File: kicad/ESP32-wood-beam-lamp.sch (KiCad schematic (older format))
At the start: 41 parts, among them J1 Screw_Terminal_01x05, J2 Screw_Terminal_01x05, J3 Conn_01x05_Male, J4 3.3 V, Q1 IRLZ44N, Q2 IRLZ44N, SW1 Flash, SW2 Reset, U1 TLV70233_SOT23-5, U2 ESP-WROOM-32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

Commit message: added BMP280
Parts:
- removed TP7: Test_Point, TestPoint:TestPoint_Pad_D1.0mm, symbol ESP32-wroom:Test_Point-Connector
- removed U4: Si7060-00, Package_TO_SOT_SMD:SOT-23-5, symbol ESP32-wroom:Si7060-module
- added U4: BMP280, symbol BMP280:BMP280
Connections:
- net labels removed: Alert2
- wire segments 146 -> 143
- no-connect marks 29 -> 30
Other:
- note removed: "Near Load Resistor\nAdress 00"
- moved on the sheet: C8
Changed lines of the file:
@@
-$EndComp
-$Comp
-L ESP32-wroom:Si7060-module U4
-U 1 1 5B338E05
-P 9150 4400
-F 0 "U4" H 9591 4471 50  0000 L CNN
-F 1 "Si7060-00" H 9591 4380 50  0000 L CNN
-F 2 "Package_TO_SOT_SMD:SOT-23-5" H 9150 4000 50  0001 C CNN
-F 3 "https://www.silabs.com/documents/public/data-sheets/Si7050-1-3-4-5-A20.pdf" H 8950 4700 50  0001 C CNN
-	1    9150 4400
-	1    0    0    -1
 $EndComp
 $Comp
@@
 L power:GND #PWR023
 U 1 1 5B340497
-P 9150 4800
-F 0 "#PWR023" H 9150 4550 50  0001 C CNN
-F 1 "GND" H 9155 4627 50  0000 C CNN
-F 2 "" H 9150 4800 50  0001 C CNN
-F 3 "" H 9150 4800 50  0001 C CNN
-	1    9150 4800
-	1    0    0    -1
-$EndComp
-Wire Wire Line
-	9150 4800 9150 4700
+P 9100 4800
+F 0 "#PWR023" H 9100 4550 50  0001 C CNN
+F 1 "GND" H 9105 4627 50  0000 C CNN
+F 2 "" H 9100 4800 50  0001 C CNN
+F 3 "" H 9100 4800 50  0001 C CNN
+	1    9100 4800
+	1    0    0    -1
+$EndComp
 $Comp
 L Device:R R12
@@
 $EndComp
 Wire Wire Line
-	8750 4300 8600 4300
+	8900 4300 8600 4300
 Wire Wire Line
 	8400 3800 8400 3900
 Wire Wire Line
 	8600 3800 8600 3900
-Wire Wire Line
-	9150 4050 9150 4000
-Wire Wire Line
-	9150 3800 8600 3800
 Connection ~ 8600 3800
 Wire Wire Line
@@
 Connection ~ 8400 4400
 Wire Wire Line
-	8400 4400 8750 4400
+	8400 4400 8900 4400
 Wire Wire Line
 	8600 4200 8600 4300
@@
 Wire Wire Line
 	8600 4300 8300 4300
-Text Label 9650 4550 0    50   ~ 0
-Alert2
-Text Label 3750 5200 0    50   ~ 0
-Alert2
-Wire Wire Line
-	3750 5200 3550 5200
 $Comp
 L power:GND #PWR010
@@
 L Device:C C8
 U 1 1 5B410ADA
-P 9600 4000
-F 0 "C8" H 9715 4046 50  0000 L CNN
-F 1 "100n" H 9715 3955 50  0000 L CNN
-F 2 "Capacitor_SMD:C_0603_1608Metric" H 9638 3850 50  0001 C CNN
-F 3 "~" H 9600 4000 50  0001 C CNN
-	1    9600 4000
+P 9650 3800
+F 0 "C8" H 9765 3846 50  0000 L CNN
+F 1 "100n" H 9765 3755 50  0000 L CNN
+F 2 "Capacitor_SMD:C_0603_1608Metric" H 9688 3650 50  0001 C CNN
+F 3 "~" H 9650 3800 50  0001 C CNN
+	1    9650 3800
 	0    1    1    0
 $EndComp
@@
 L power:GND #PWR025
 U 1 1 5B415F17
-P 9850 4000
-F 0 "#PWR025" H 9850 3750 50  0001 C CNN
-F 1 "GND" H 9855 3827 50  0000 C CNN
-F 2 "" H 9850 4000 50  0001 C CNN
-F 3 "" H 9850 4000 50  0001 C CNN
-	1    9850 4000
+P 9850 3800
+F 0 "#PWR025" H 9850 3550 50  0001 C CNN
+F 1 "GND" H 9855 3627 50  0000 C CNN
+F 2 "" H 9850 3800 50  0001 C CNN
+F 3 "" H 9850 3800 50  0001 C CNN
+	1    9850 3800
 	0    -1   -1   0
 $EndComp
 Wire Wire Line
-	9450 4000 9150 4000
-Connection ~ 9150 4000
-Wire Wire Line
-	9150 4000 9150 3800
-Wire Wire Line
-	9750 4000 9850 4000
-Text Notes 9450 3850 0    50   ~ 0
-Near Load Resistor\nAdress 00
+	9800 3800 9850 3800
 Text Notes 600  650  0    50   ~ 0
 Voltage Regulator
@@
 Wire Wire Line
 	3850 1350 3450 1350
-$Comp
-L ESP32-wroom:Test_Point-Connector TP7
-U 1 1 5B63D623
-P 9900 4550
-F 0 "TP7" H 9958 4670 50  0000 L CNN
-F 1 "Test_Point" H 9958 4579 50  0000 L CNN
-F 2 "TestPoint:TestPoint_Pad_D1.0mm" H 10100 4550 50  0001 C CNN
-F 3 "~" H 10100 4550 50  0001 C CNN
-	1    9900 4550
-	0    1    1    0
-$EndComp
-Wire Wire Line
-	9550 4550 9900 4550
 Wire Wire Line
 	3550 3200 3400 3200
@@
 SDA
 Wire Notes Line
-	8050 3150 10900 3150
+	8050 3150 10300 3150
 Wire Notes Line
-	10900 3150 10900 6300
+	10300 3150 10300 5150
 Wire Notes Line
-	10900 6300 8050 6300
+	10300 5150 8050 5150
 Wire Notes Line
-	8050 6300 8050 3150
+	8050 5150 8050 3150
 Text Notes 8100 3250 0    50   ~ 0
 Temperature Sensors
@@
 NoConn ~ 5050 2950
 NoConn ~ 5050 2850
+Wire Wire Line
+	8600 3800 9100 3800
+$Comp
+L BMP280:BMP280 U4
+U 1 1 5C0B3D06
+P 9050 4350
+F 0 "U4" H 9277 4421 50  0000 L CNN
+F 1 "BMP280" H 9277 4330 50  0000 L CNN
+F 2 "" H 9050 4350 50  0001 C CNN
+F 3 "" H 9050 4350 50  0001 C CNN
+	1    9050 4350
+	1    0    0    -1
+$EndComp
+Wire Wire Line
+	9100 4750 9100 4800
+Wire Wire Line
+	9100 3900 9100 3800
+Connection ~ 9100 3800
+Wire Wire Line
+	9100 3800 9500 3800
+NoConn ~ 3550 5200
 $EndSCHEMATC

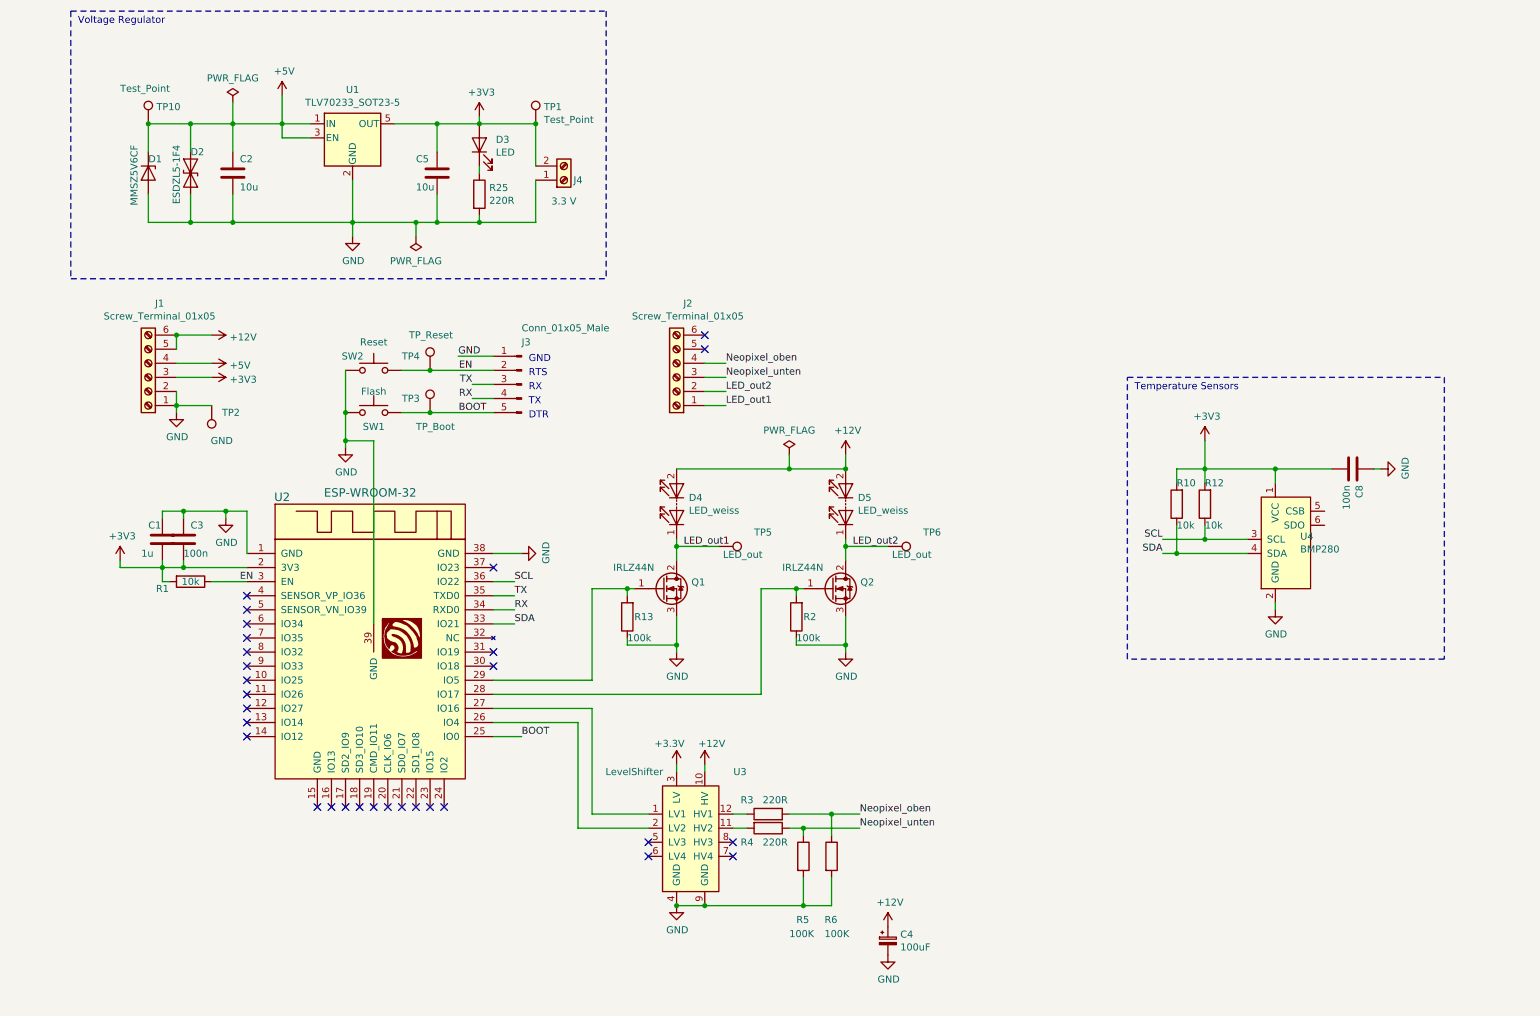
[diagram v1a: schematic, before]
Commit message: Nextion connector added
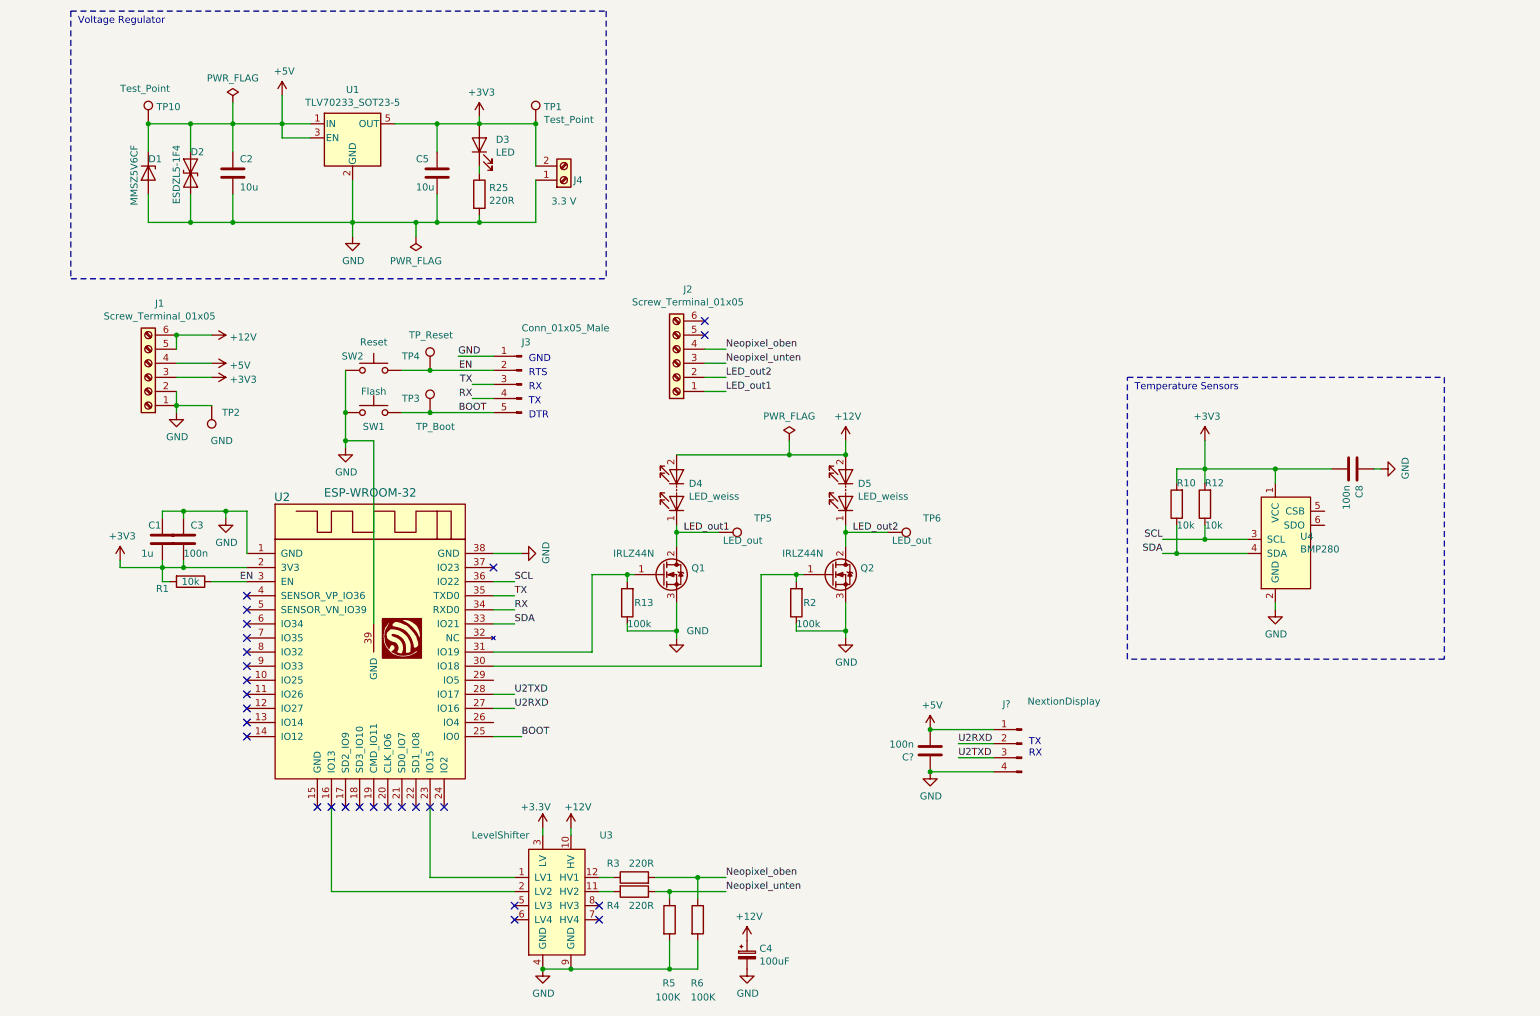
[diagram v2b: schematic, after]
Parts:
- added C?: 100n, Capacitor_SMD:C_0603_1608Metric, symbol Device:C
- added J?: NextionDisplay, symbol Connector:Conn_01x04_Male
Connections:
- net +5V: now also C?.2, J?.1 (Pin_1)
- net GND: now also C?.1, J?.4 (Pin_4)
- net at U2.16 (IO13): now also U3.2 (LV2)
- net at U2.23 (IO15): now also U3.1 (LV1)
- net at U2.26 (IO4): no longer U3.2 (LV2)
- net U2RXD: now reaches U2.27 (IO16)
- net U2RXD: now also J?.2 (Pin_2); no longer U3.1 (LV1)
- net at Q2.1 (G), R2.2: now also U2.30 (IO18); no longer U2.28 (IO17)
- net at Q1.1 (G), R13.2: now also U2.31 (IO19); no longer U2.29 (IO5)
- new net U2TXD: J?.3 (Pin_3), U2.28 (IO17)
- no-connect marks 30 -> 28
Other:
- note added: "TX\nRX"
- moved on the sheet: C4, D4, D5, J2, Q1, Q2, R13, R2, R3, R4, R5, R6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

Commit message: Nextion connector added
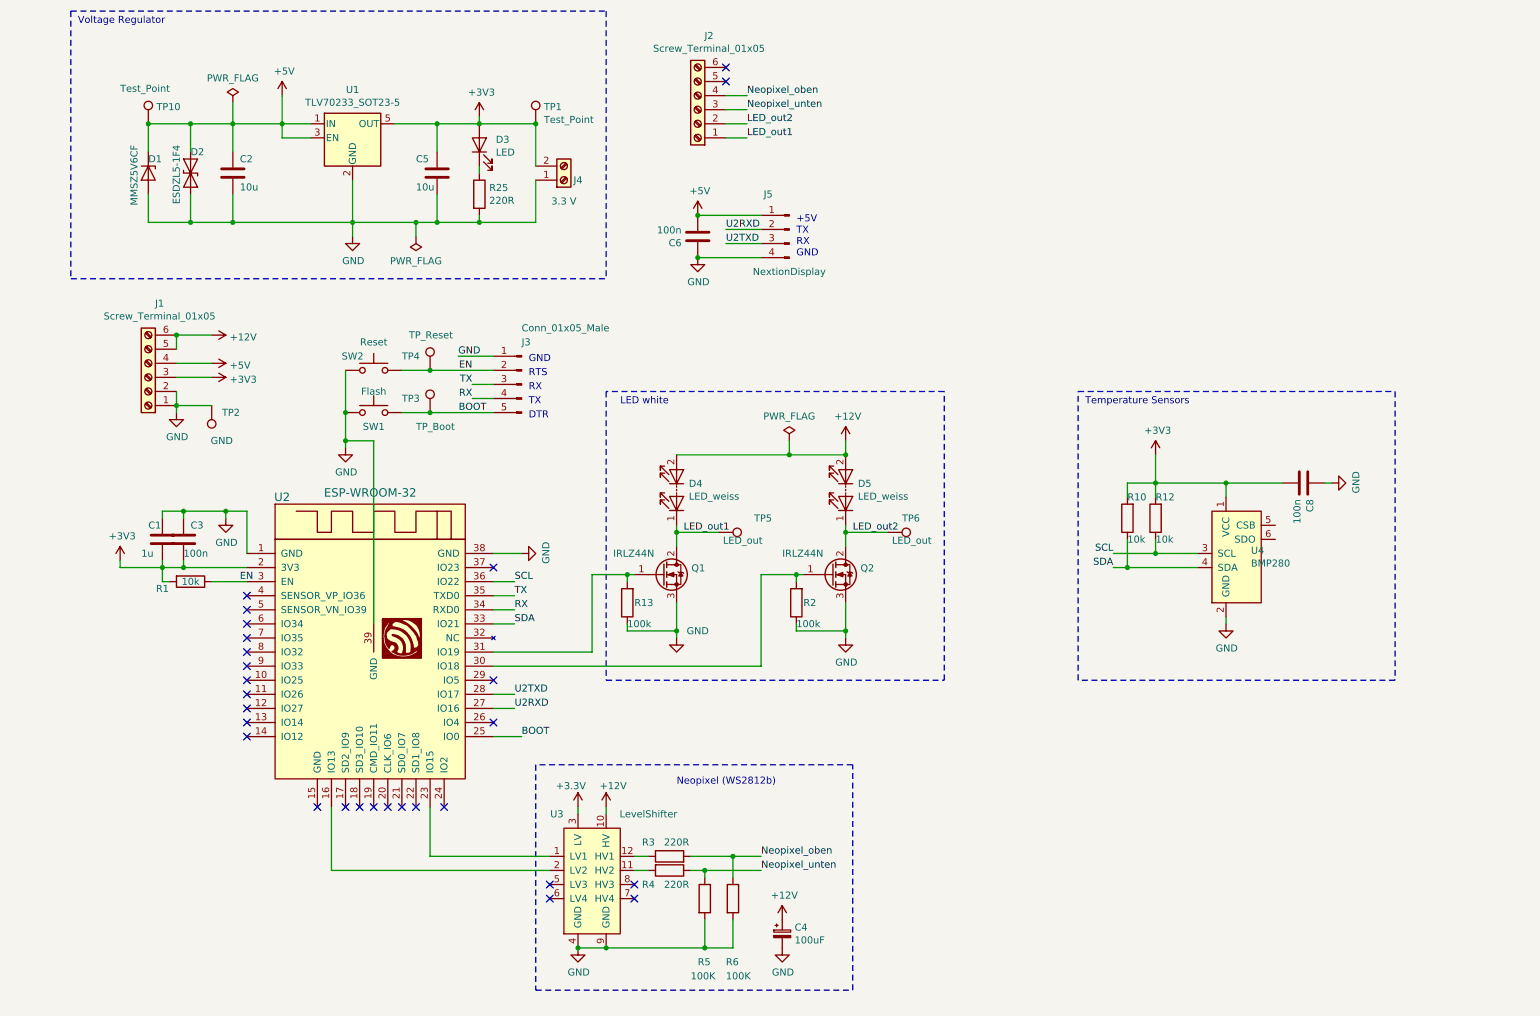
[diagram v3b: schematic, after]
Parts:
- gave numbers to parts that had none: 2
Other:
- note added: "+5V\nTX\nRX\nGND"
- note added: "LED white"
- note added: "Neopixel (WS2812b)"
- note removed: "TX\nRX"
- moved on the sheet: C4, C6, C8, J2, J5, R10, R12, R3, R4, R5, R6, U3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

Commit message: IRF3708
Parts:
- Q1, Q2: value IRLZ44N -> IRF3708
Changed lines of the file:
@@
 P 4750 4550
 F 0 "Q1" H 4955 4596 50  0000 L CNN
-F 1 "IRLZ44N" H 4400 4700 50  0000 L CNN
+F 1 "IRF3708" H 4400 4700 50  0000 L CNN
 F 2 "Package_TO_SOT_SMD:SOT-23" H 4950 4650 50  0001 C CNN
 F 3 "~" H 4750 4550 50  0001 C CNN
@@
 P 5950 4550
 F 0 "Q2" H 6155 4596 50  0000 L CNN
-F 1 "IRLZ44N" H 5600 4700 50  0000 L CNN
+F 1 "IRF3708" H 5600 4700 50  0000 L CNN
 F 2 "Package_TO_SOT_SMD:SOT-23" H 6150 4650 50  0001 C CNN
 F 3 "~" H 5950 4550 50  0001 C CNN

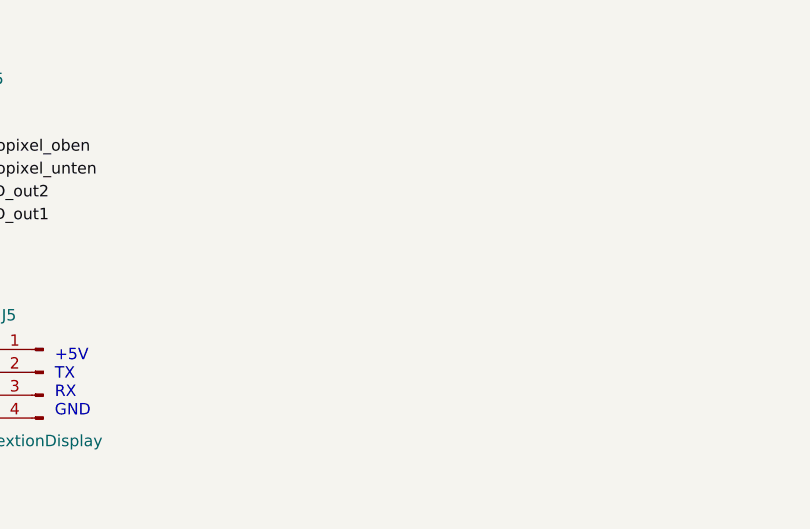
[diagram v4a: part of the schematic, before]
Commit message: USB Connector added
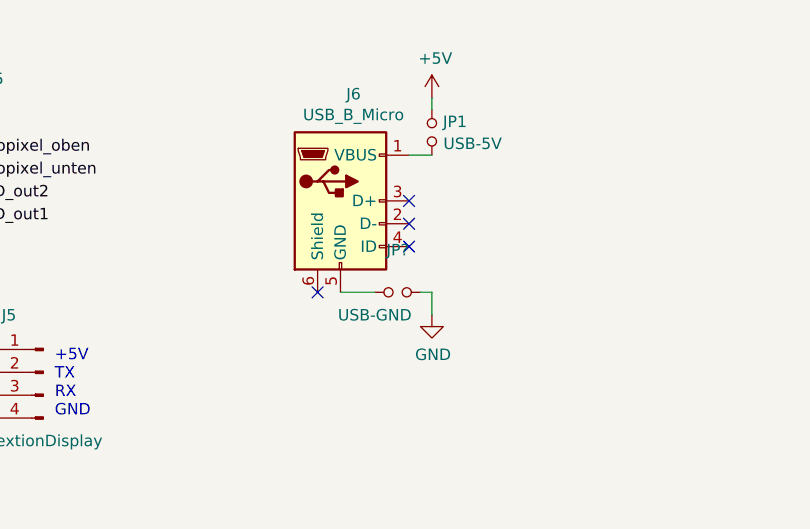
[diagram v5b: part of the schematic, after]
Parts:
- added J6: USB_B_Micro, symbol Connector:USB_B_Micro
- added JP1: USB-5V, symbol Device:Jumper_NO_Small
- added JP?: USB-GND, symbol Device:Jumper_NO_Small
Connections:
- net +5V: now also JP1.1
- net GND: now also JP?.1
- new net: J6.1 (VBUS), JP1.2
- new net: J6.5 (GND), JP?.2
- no-connect marks 28 -> 32
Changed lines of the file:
@@
 Wire Notes Line
 	3850 5900 3850 7500
+$Comp
+L Device:Jumper_NO_Small JP1
+U 1 1 5BE3BEB6
+P 7350 1050
+F 0 "JP1" V 7304 1098 50  0000 L CNN
+F 1 "USB-5V" V 7400 1100 50  0000 L CNN
+F 2 "" H 7350 1050 50  0001 C CNN
+F 3 "~" H 7350 1050 50  0001 C CNN
+	1    7350 1050
+	0    1    1    0
+$EndComp
+$Comp
+L Connector:USB_B_Micro J6
+U 1 1 5BE3C6FD
+P 6950 1350
+F 0 "J6" H 7007 1817 50  0000 C CNN
+F 1 "USB_B_Micro" H 7007 1726 50  0000 C CNN
+F 2 "" H 7100 1300 50  0001 C CNN
+F 3 "~" H 7100 1300 50  0001 C CNN
+	1    6950 1350
+	1    0    0    -1
+$EndComp
+Wire Wire Line
+	7250 1150 7350 1150
+$Comp
+L power:+5V #PWR0103
+U 1 1 5BE4C1E4
+P 7350 900
+F 0 "#PWR0103" H 7350 750 50  0001 C CNN
+F 1 "+5V" H 7365 1073 50  0000 C CNN
+F 2 "" H 7350 900 50  0001 C CNN
+F 3 "" H 7350 900 50  0001 C CNN
+	1    7350 900
+	1    0    0    -1
+$EndComp
+Wire Wire Line
+	7350 900  7350 950
+NoConn ~ 7250 1350
+NoConn ~ 7250 1450
+NoConn ~ 7250 1550
+NoConn ~ 6850 1750
+$Comp
+L power:GND #PWR0104
+U 1 1 5BE75942
+P 7350 1850
+F 0 "#PWR0104" H 7350 1600 50  0001 C CNN
+F 1 "GND" H 7355 1677 50  0000 C CNN
+F 2 "" H 7350 1850 50  0001 C CNN
+F 3 "" H 7350 1850 50  0001 C CNN
+	1    7350 1850
+	1    0    0    -1
+$EndComp
+$Comp
+L Device:Jumper_NO_Small JP?
+U 1 1 5BE7BE7C
+P 7200 1750
+F 0 "JP?" H 7200 1565 50  0000 C CNN
+F 1 "USB-GND" H 7300 1850 50  0000 C CNN
+F 2 "" H 7200 1750 50  0001 C CNN
+F 3 "~" H 7200 1750 50  0001 C CNN
+	1    7200 1750
+	-1   0    0    1
+$EndComp
+Wire Wire Line
+	6950 1750 7100 1750
+Wire Wire Line
+	7300 1750 7350 1750
+Wire Wire Line
+	7350 1750 7350 1850
 $EndSCHEMATC

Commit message: footprints added
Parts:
- removed D4, D5: LED_weiss, LED_THT:LED_D5.0mm, symbol Device:LED_Series
- removed J4: 3.3 V, symbol Connector:Screw_Terminal_01x02
- added D4, D5: LED, LED_SMD:LED_1210_3225Metric_Pad1.42x2.65mm_HandSolder, symbol Device:LED
- added J4: Conn_01x02, Connector_PinHeader_2.54mm:PinHeader_1x02_P2.54mm_Vertical, symbol Connector_Generic:Conn_01x02
- added J7: AUX, Connector_PinHeader_2.54mm:PinHeader_1x05_P2.54mm_Horizontal, symbol Connector:Conn_01x05_Male
- added R7, R8: 680R, Resistor_SMD:R_1206_3216Metric_Pad1.42x1.75mm_HandSolder, symbol Device:R
- C1, C2, C5: footprint Capacitor_SMD:C_0805_2012Metric -> Capacitor_SMD:C_1206_3216Metric_Pad1.42x1.75mm_HandSolder
- C3, C6, C8: footprint Capacitor_SMD:C_0603_1608Metric -> Capacitor_SMD:C_1206_3216Metric_Pad1.42x1.75mm_HandSolder
- C4: footprint (none) -> Capacitor_THT:CP_Radial_D7.5mm_P2.50mm
- D3: footprint (none) -> LED_SMD:LED_1210_3225Metric_Pad1.42x2.65mm_HandSolder
- J3: value Conn_01x05_Male -> Serial-Prog
- J5: footprint (none) -> Connector_PinHeader_2.54mm:PinHeader_1x04_P2.54mm_Vertical
- J6: footprint (none) -> Connector_USB:USB_Micro-B_Molex-105017-0001
- JP1: footprint (none) -> Connector_PinHeader_2.54mm:PinHeader_1x02_P2.54mm_Vertical
- JP2: renamed from JP?; footprint (none) -> Connector_PinHeader_2.54mm:PinHeader_1x02_P2.54mm_Vertical
- Q1, Q2: footprint Package_TO_SOT_SMD:SOT-23 -> Package_TO_SOT_THT:TO-220-3_Vertical
- R1, R10, R12, R13, R2: footprint Resistor_SMD:R_0603_1608Metric -> Resistor_SMD:R_1206_3216Metric_Pad1.42x1.75mm_HandSolder
- R25, R3, R4, R5, R6: footprint (none) -> Resistor_SMD:R_1206_3216Metric_Pad1.42x1.75mm_HandSolder
- SW1, SW2: footprint (none) -> w_switch:PCB_PUSH; symbol Switch:SW_Push -> Switch:SW_Push_Dual
- TP1, TP2, TP3, TP4, TP5, TP6: footprint TestPoint:TestPoint_Pad_D1.0mm -> TestPoint:TestPoint_Pad_D1.5mm
- TP7: renamed from TP10; footprint TestPoint:TestPoint_Pad_D1.0mm -> TestPoint:TestPoint_Pad_D1.5mm
- U3: footprint (none) -> Package_DIP:DIP-12_W10.16mm_LongPads
- U4: footprint (none) -> Connector_PinSocket_2.54mm:PinSocket_1x06_P2.54mm_Vertical
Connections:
- net +12V: now also R7.1, R8.1
- net +3V3: now also J4.1 (Pin_1), J7.1 (Pin_1)
- net BOOT: now also SW1.4
- net EN: now also SW2.4
- net GND: now also SW1.3, SW2.3, J4.2 (Pin_2), J7.5 (Pin_5)
- net LED_out1: now also D4.1 (K)
- net LED_out2: now also D5.1 (K)
- net IO25: now reaches U2.10 (IO25)
- net IO25: now also J7.3 (Pin_3)
- net IO26: now reaches U2.11 (IO26)
- net IO26: now also J7.4 (Pin_4)
- net IO33: now reaches U2.9 (IO33)
- net IO33: now also J7.2 (Pin_2)
- new net: D4.2 (A), R7.2
- new net: D5.2 (A), R8.2
- no-connect marks 32 -> 31
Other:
- moved on the sheet: J3, Q1, Q2, R13, R2, TP3, TP4, TP5, TP6
